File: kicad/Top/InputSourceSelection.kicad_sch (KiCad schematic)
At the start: 26 parts

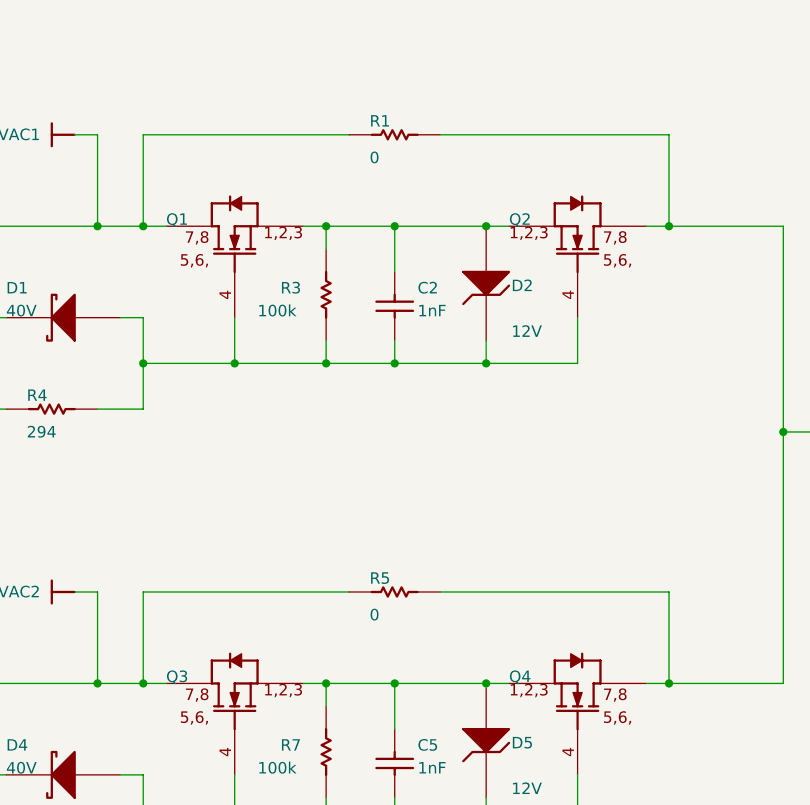
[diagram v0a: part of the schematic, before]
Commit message: Properly synced pcb to schematic
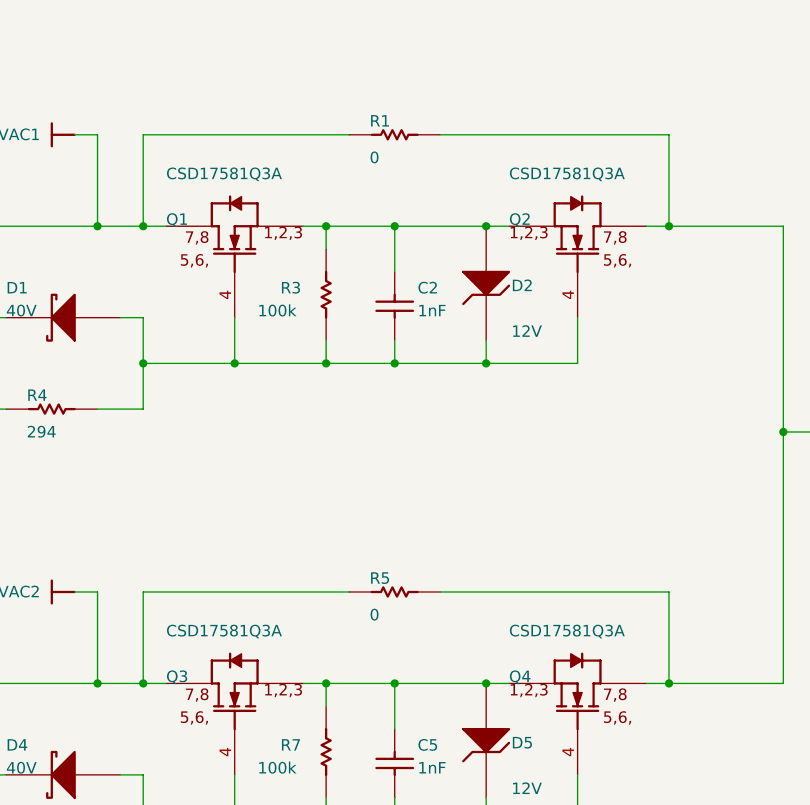
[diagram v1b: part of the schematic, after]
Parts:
- C1, C4: value ~ -> CMP-0008217-2; footprint 0805L -> AltiumImports:0805L
- C2, C5: value ~ -> GRM1555C1H102FA01D; footprint 0402 -> AltiumImports:0402
- D1, D4: value ~ -> CMP-0028378-3; footprint SOD-523 -> AltiumImports:SOD-523
- D2, D5: value ~ -> BZT52C12T-7; footprint SOD-523 -> AltiumImports:SOD-523
- J1, J2: value ~ -> ED120/2DS; footprint On-Shore_ED120_2DS -> AltiumImports:On-Shore_ED120_2DS
- Q1, Q2, Q3, Q4: value ~ -> CSD17581Q3A; footprint DNH0008A -> AltiumImports:DNH0008A
- R1, R5: value ~ -> 5106; footprint 5106 -> AltiumImports:5106
- R2, R6: value ~ -> WSL2010R0100FEA18; footprint 2010 -> AltiumImports:2010
- R3, R7: value ~ -> RC0402FR-07100KL; footprint 0402 -> AltiumImports:0402
- R4, R9: value ~ -> CRCW0603294RFKEA; footprint 0603 -> AltiumImports:0603
- TP1, TP2, TP7, TP8: value ~ -> CMP-0055139-1; footprint Keystone5002 -> AltiumImports:Keystone5002
